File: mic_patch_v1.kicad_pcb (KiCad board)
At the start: 2 copper layers, 30 x 30 mm, 53 parts, among them J1 Conn_ARM_SWD_TagConnect_TC203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, J3 J_000001, J4 Micro_SD_Card, J5 J_000002, SW1 SW_000001, SW2 SW_000001, U1 NORA-B106-00B, U2 PWR_nPM1100-QDXX, U3 ADAU7002ACBZ-R7, Y1 CLK_0003

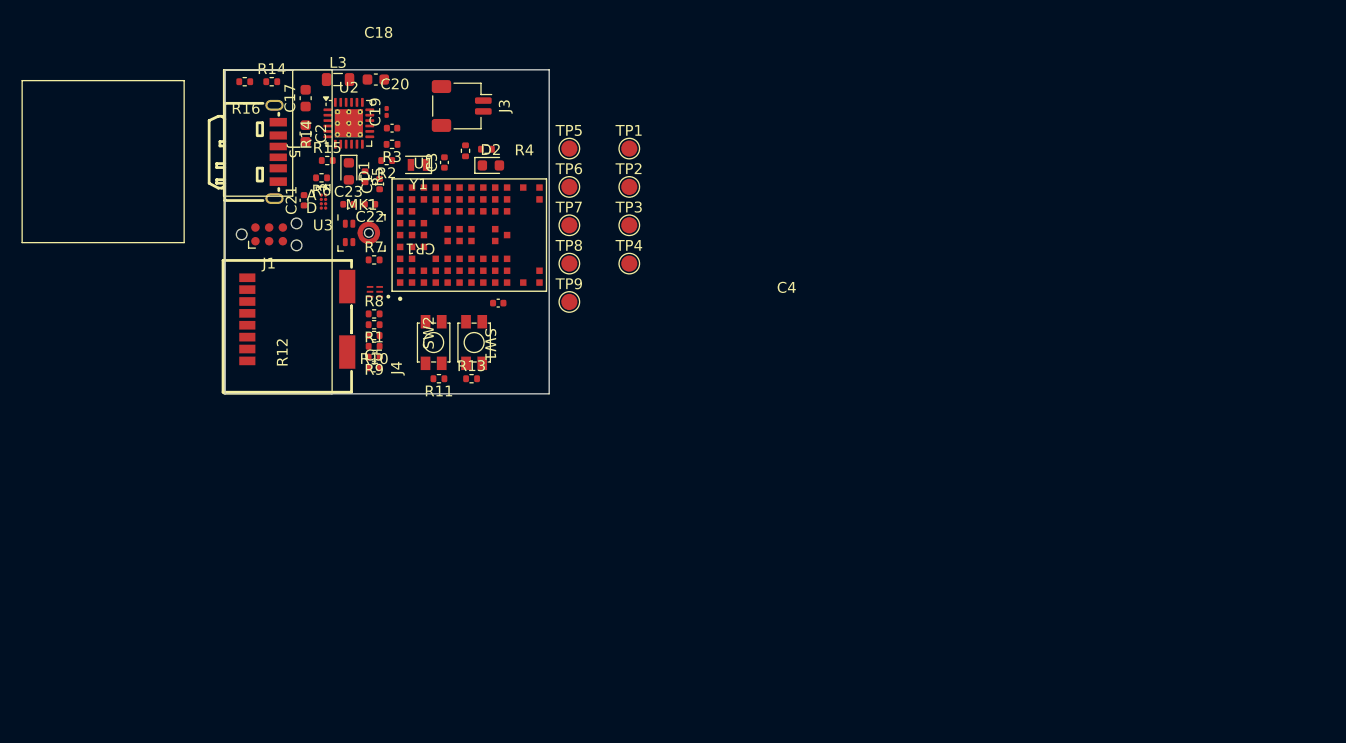
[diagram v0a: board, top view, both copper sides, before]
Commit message: sketched out board dimensions
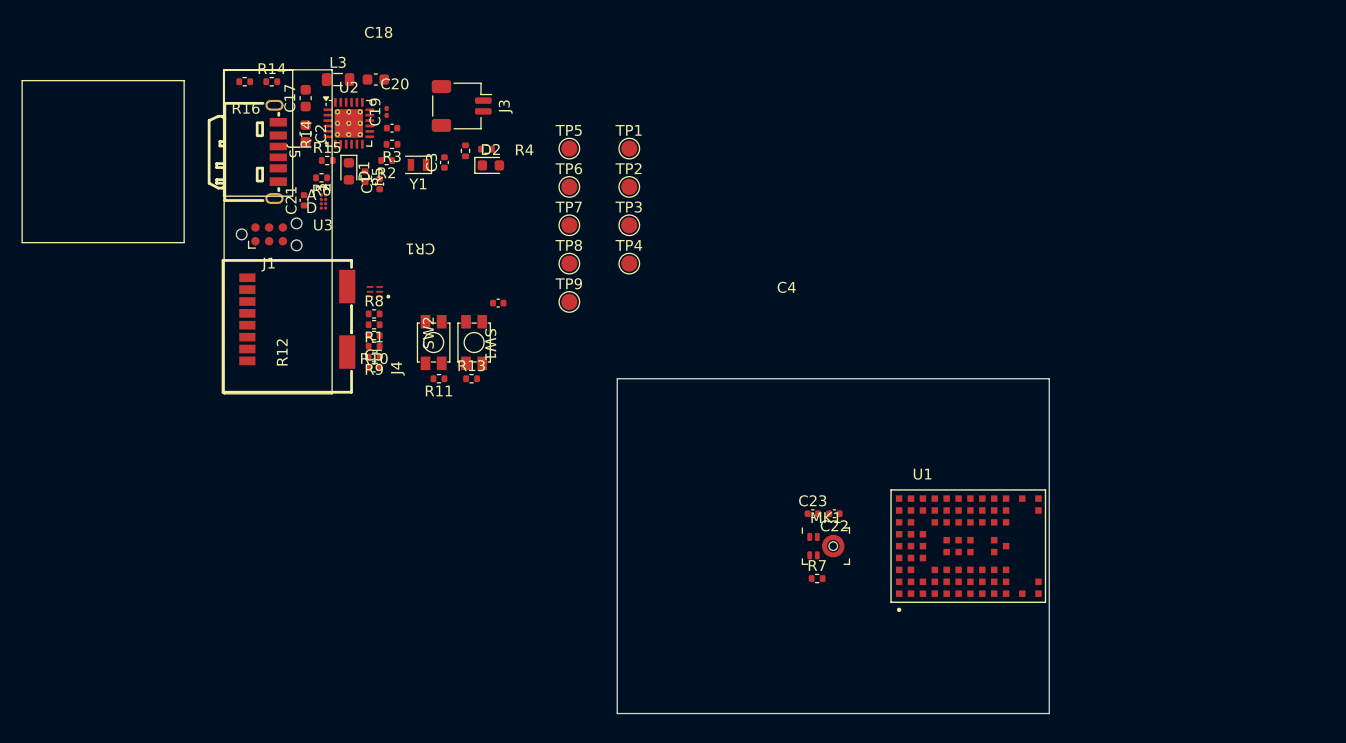
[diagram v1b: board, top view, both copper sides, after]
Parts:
- moved U1 54.4 mm to (161.6, 105.0)
- moved MK1 51.9 mm to (149.3, 105.0)
- moved C22 51.7 mm to (150.1, 102.0)
- moved C23 51.7 mm to (148.1, 102.0)
- moved R7 50.5 mm to (148.5, 108.0)
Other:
- board size 30 x 30 mm -> 40 x 31 mm

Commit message: poured ground layer added RF keep out
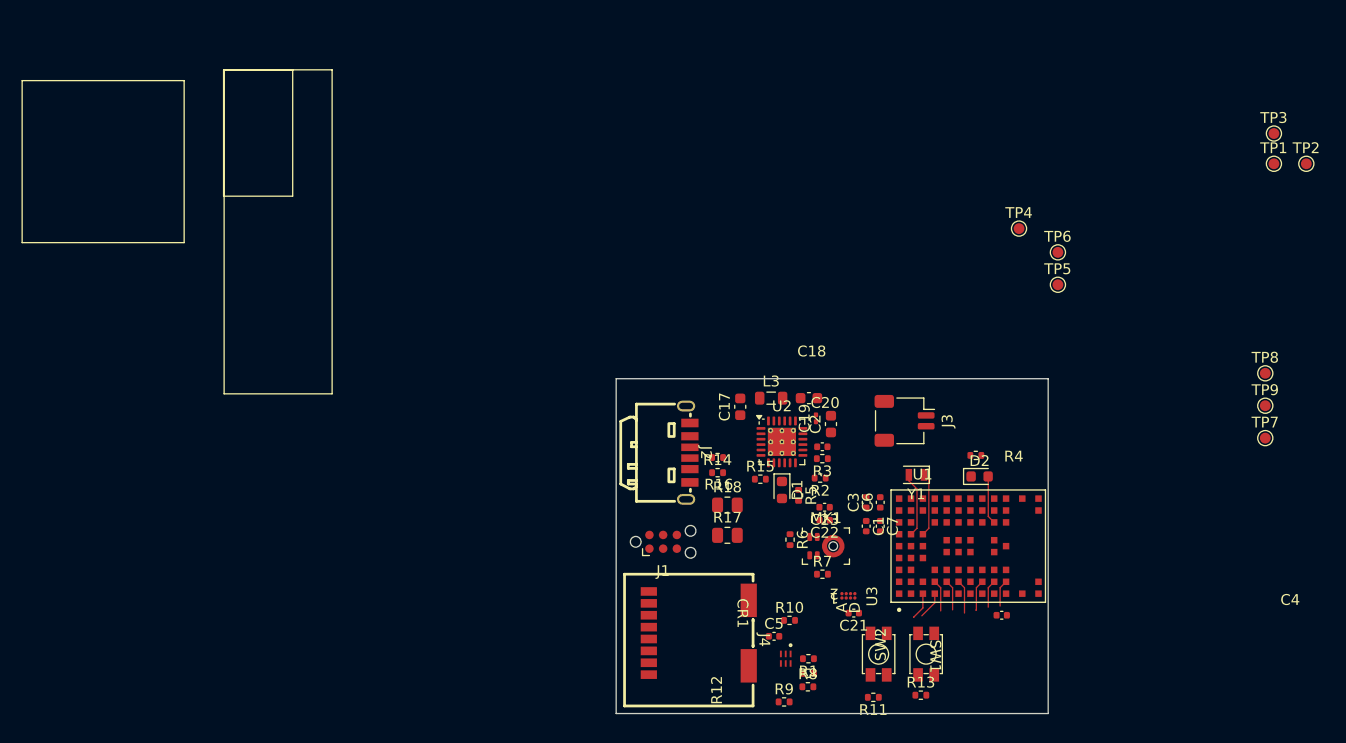
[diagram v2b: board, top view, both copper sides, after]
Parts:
- removed J5: J_000002, mic_patch_parts:C5260493
- removed the R14 at (116.0, 68.4)
- added C6: C_00001, Capacitor_SMD:C_0402_1005Metric, F.Cu at (154.3, 101.0)
- added C7: C_00001, Capacitor_SMD:C_0402_1005Metric, F.Cu at (154.3, 103.2)
- added J2: J_000002, mic_patch_parts:J_000002, F.Cu at (136.6, 96.3)
- added R17: R_00001, Resistor_SMD:R_0805_2012Metric, F.Cu at (140.2, 104.0)
- added R18: R_00001, Resistor_SMD:R_0805_2012Metric, F.Cu at (140.2, 101.2)
- TP1, TP2, TP3, TP4, TP5, TP6, TP7, TP8, TP9: footprint TestPoint:TestPoint_Pad_D1.5mm -> TestPoint:TestPoint_Pad_D1.0mm
- moved TP7 67.4 mm to (190.0, 95.0)
- moved TP8 65.2 mm to (190.0, 89.0)
- moved TP9 65.1 mm to (190.0, 92.0)
- moved C21 63.7 mm to (151.9, 111.2), turned to 180 degrees
- moved TP2 62.7 mm to (193.8, 69.6)
- moved U3 60.8 mm to (151.4, 109.6), turned to 90 degrees
- moved TP3 60.3 mm to (190.8, 66.8)
- moved TP1 59.7 mm to (190.8, 69.6)
- moved R16 55.9 mm to (139.3, 96.8)
- moved C2 55.6 mm to (149.8, 93.7), turned to 90 degrees
- moved C1 55.1 mm to (153.1, 103.2), turned to -90 degrees
- moved R14 54.9 mm to (139.3, 98.2)
- moved C4 54.9 mm to (165.6, 111.4)
- moved R6 54.8 mm to (146.0, 104.4), turned to -90 degrees
- moved Y1 54.3 mm to (157.7, 98.4)
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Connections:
- C18 pad 1: /Power/DEC_NPM -> GND
- C18 pad 2: GND -> /Power/DEC_NPM
- J4 pad 9: unconnected-(J4-SHIELD-Pad9) -> GND
- U2 pad 2: VSYS -> Net-(U2-VOUTBSET0)
- U2 pad 3: VSYS -> Net-(U2-VOUTBSET0)
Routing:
- net Net-(U1-P0.01/XL2): track 0.00 -> 6.04 mm
- net Net-(U1-P0.00/XL1): track 0.00 -> 5.91 mm
- net Net-(D2-A): track 0.00 -> 4.64 mm
- net FSYNC_LRCLK: track 0.00 -> 3.13 mm
- net DIN: track 0.00 -> 2.93 mm
- net /MCU/SWDIO: track 0.00 -> 2.90 mm
- net BCLK: track 0.00 -> 2.83 mm
- net /MCU/SWCLK: track 0.00 -> 2.58 mm
- net SD MISO: track 0.00 -> 2.55 mm
- net SD CSN: track 0.00 -> 2.55 mm
- net GND: track 0.00 -> 2.48 mm
- added copper zone on In1.Cu, net GND
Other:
- copper layers 2 -> 4

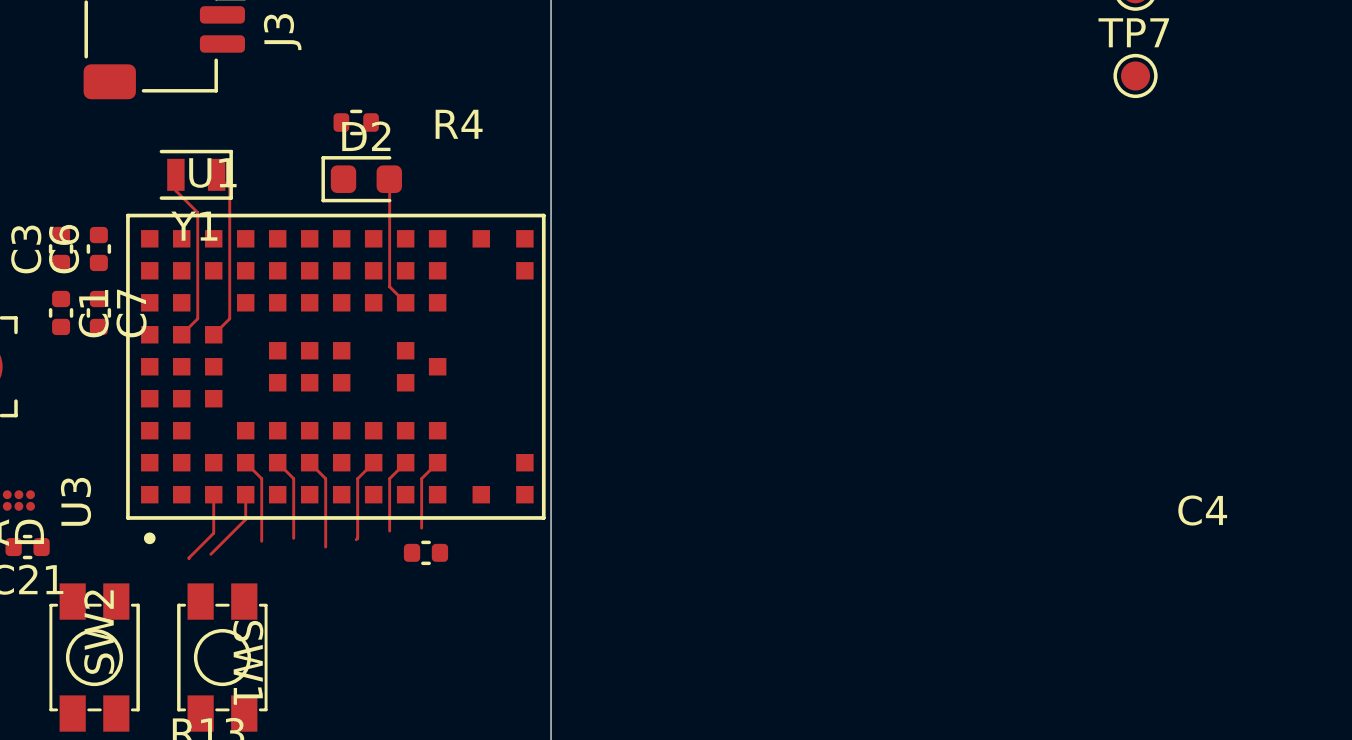
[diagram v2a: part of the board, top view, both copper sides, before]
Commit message: added RF ground plane stitching vias
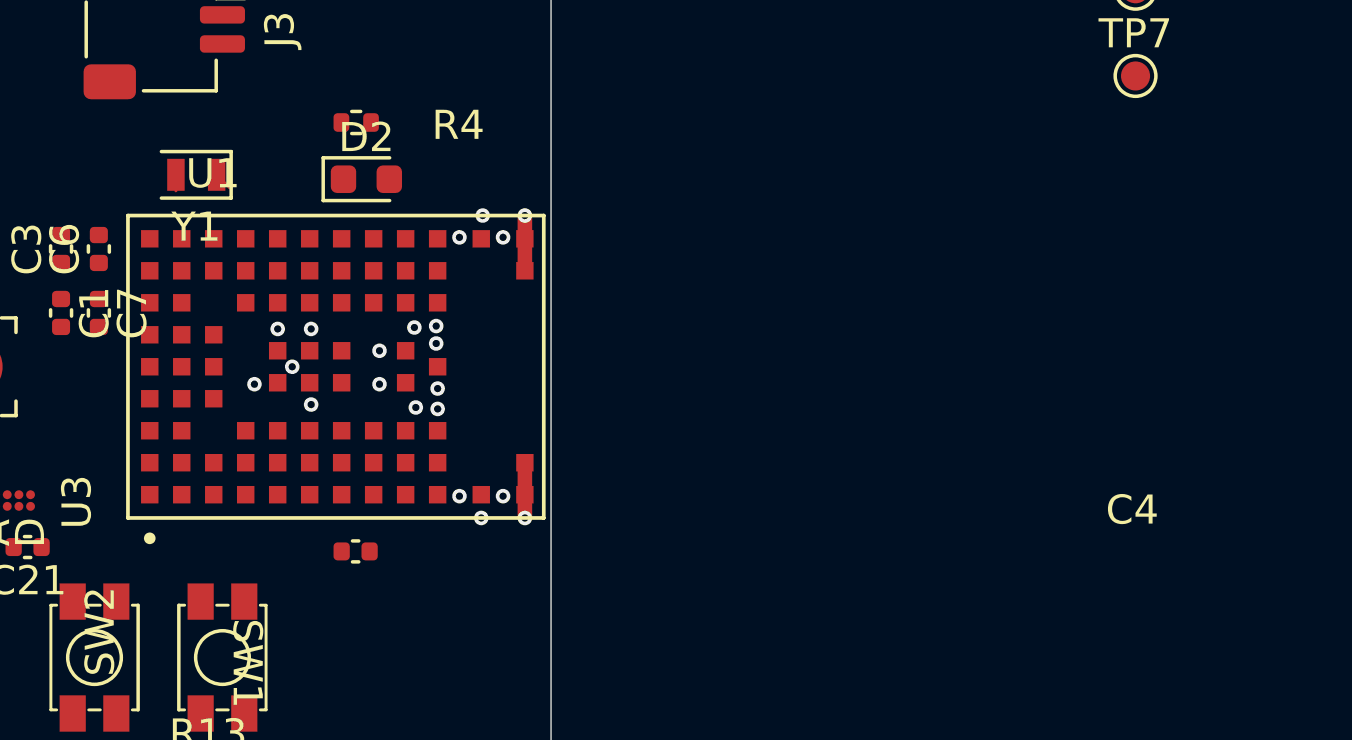
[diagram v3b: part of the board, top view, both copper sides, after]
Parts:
- moved C4 2.42 mm to (163.2, 111.3)
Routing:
- net Net-(U1-P0.01/XL2): track 6.04 -> 0.55 mm
- net Net-(U1-P0.00/XL1): track 5.91 -> 0.64 mm
- net Net-(D2-A): track 4.64 -> 0.05 mm
- net FSYNC_LRCLK: track 3.13 -> 0.00 mm
- net DIN: track 2.93 -> 0.00 mm
- net /MCU/SWDIO: track 2.90 -> 0.00 mm
- net BCLK: track 2.83 -> 0.00 mm
- net /MCU/SWCLK: track 2.58 -> 0.00 mm
- net SD MISO: track 2.55 -> 0.00 mm
- net SD CSN: track 2.55 -> 0.00 mm
- net GND: track 2.48 -> 3.80 mm, vias 0 -> 21

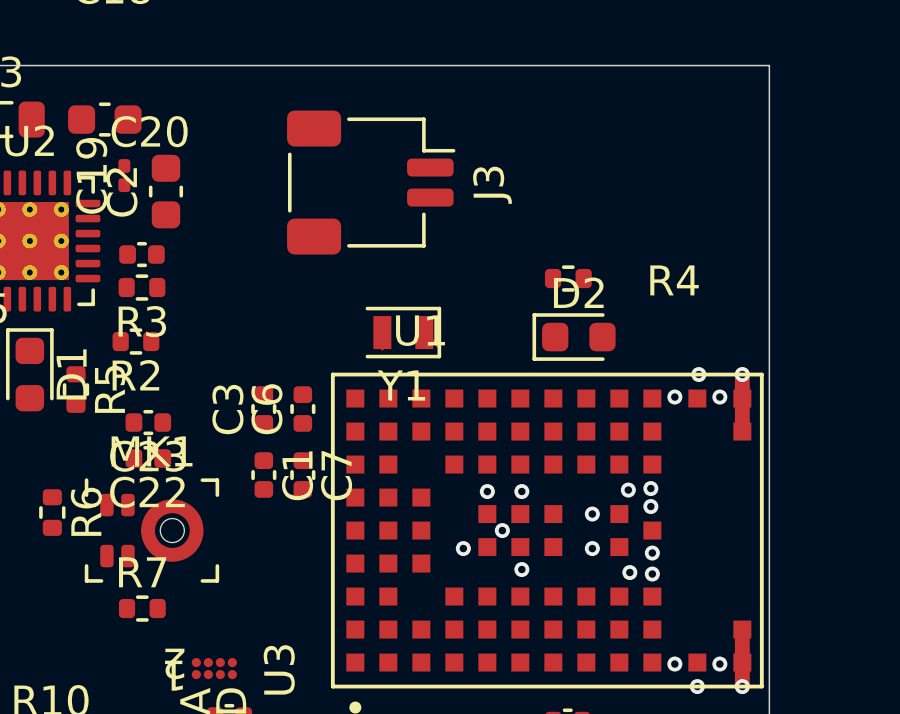
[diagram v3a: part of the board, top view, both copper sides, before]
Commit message: switched around pins for easier routing
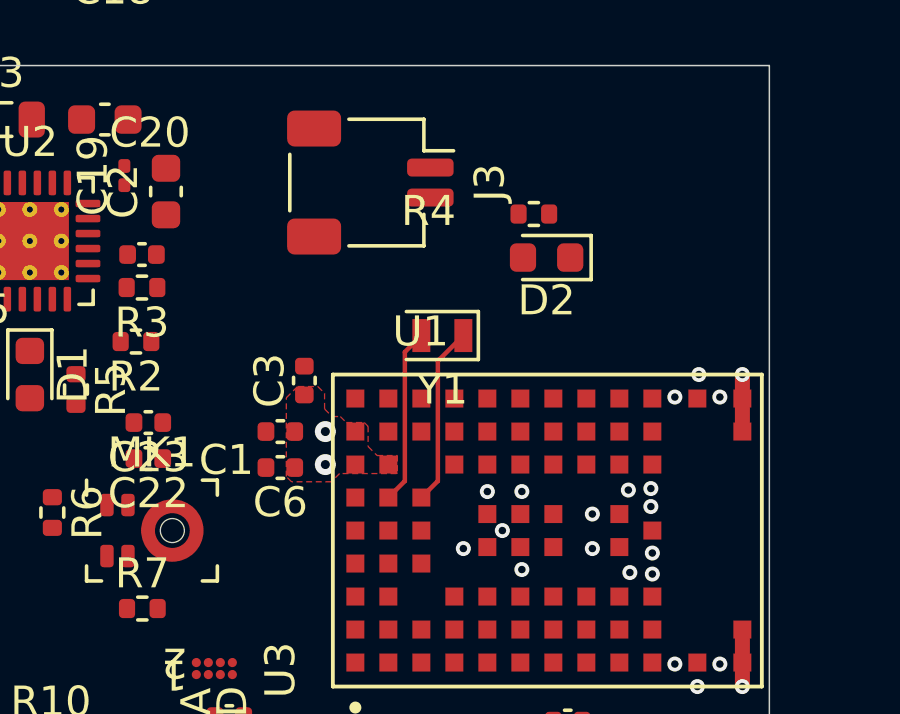
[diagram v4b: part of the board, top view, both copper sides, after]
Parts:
- removed C7: C_00001, Capacitor_SMD:C_0402_1005Metric
- moved D2 2.86 mm to (162.5, 95.9), turned to 180 degrees
- moved R4 2.44 mm to (162.1, 94.5), turned to 180 degrees
- moved C6 2.09 mm to (153.6, 102.9), turned to 180 degrees
- moved C3 1.65 mm to (154.4, 100.0)
- moved C1 1.55 mm to (153.6, 101.7), turned to 180 degrees
- moved Y1 1.30 mm to (159.0, 98.5)
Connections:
- U1 pad F9: unconnected-(U1-P1.15-PadF9) -> NPM ERROR
- U1 pad G4: NPM ERROR -> unconnected-(U1-P1.04-PadG4)
- U1 pad G9: unconnected-(U1-P1.13-PadG9) -> Net-(D2-A)
- U1 pad J7: Net-(D2-A) -> unconnected-(U1-P1.10-PadJ7)
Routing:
- net Net-(U1-P0.00/XL1): track 0.64 -> 5.98 mm
- net Net-(U1-P0.01/XL2): track 0.55 -> 5.86 mm
- net +3V0 VDD_NRF: vias 0 -> 2
- added copper zone on F.Cu, net +3V0 VDD_NRF

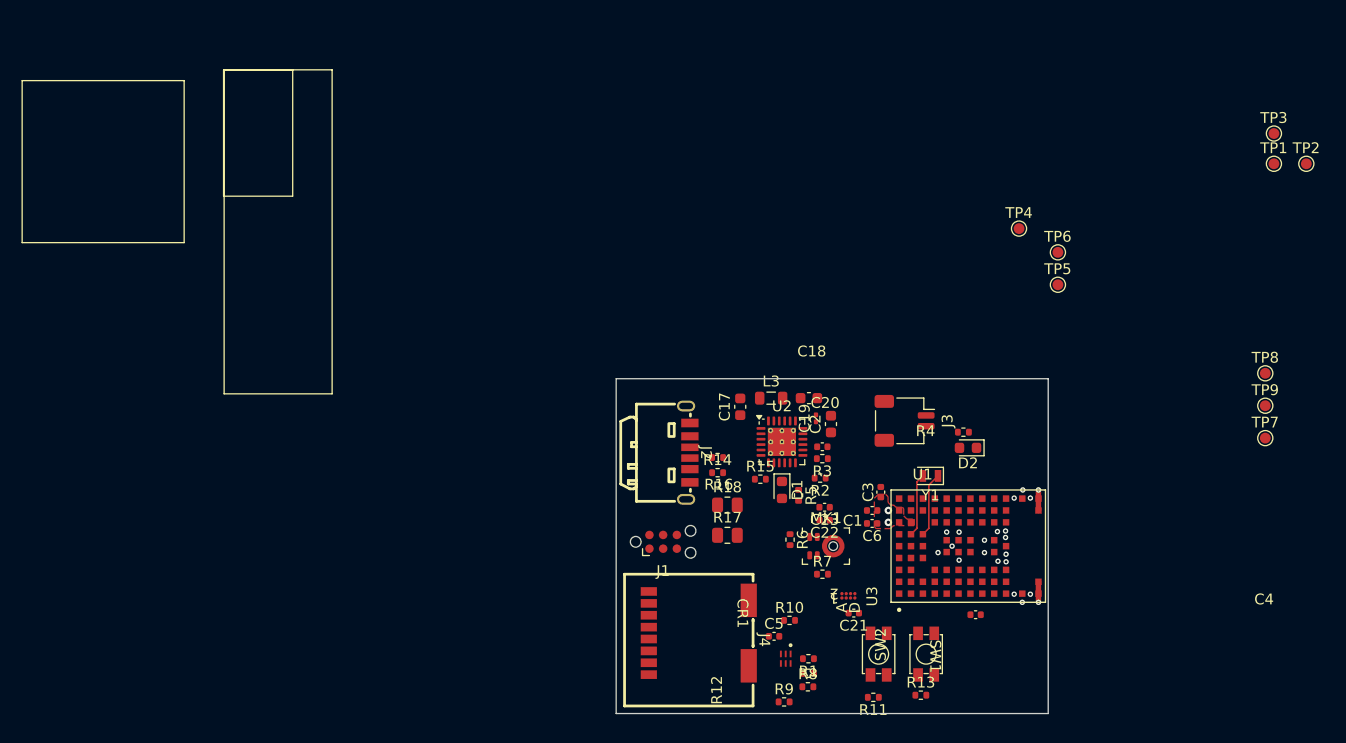
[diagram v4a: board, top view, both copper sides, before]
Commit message: routed audio
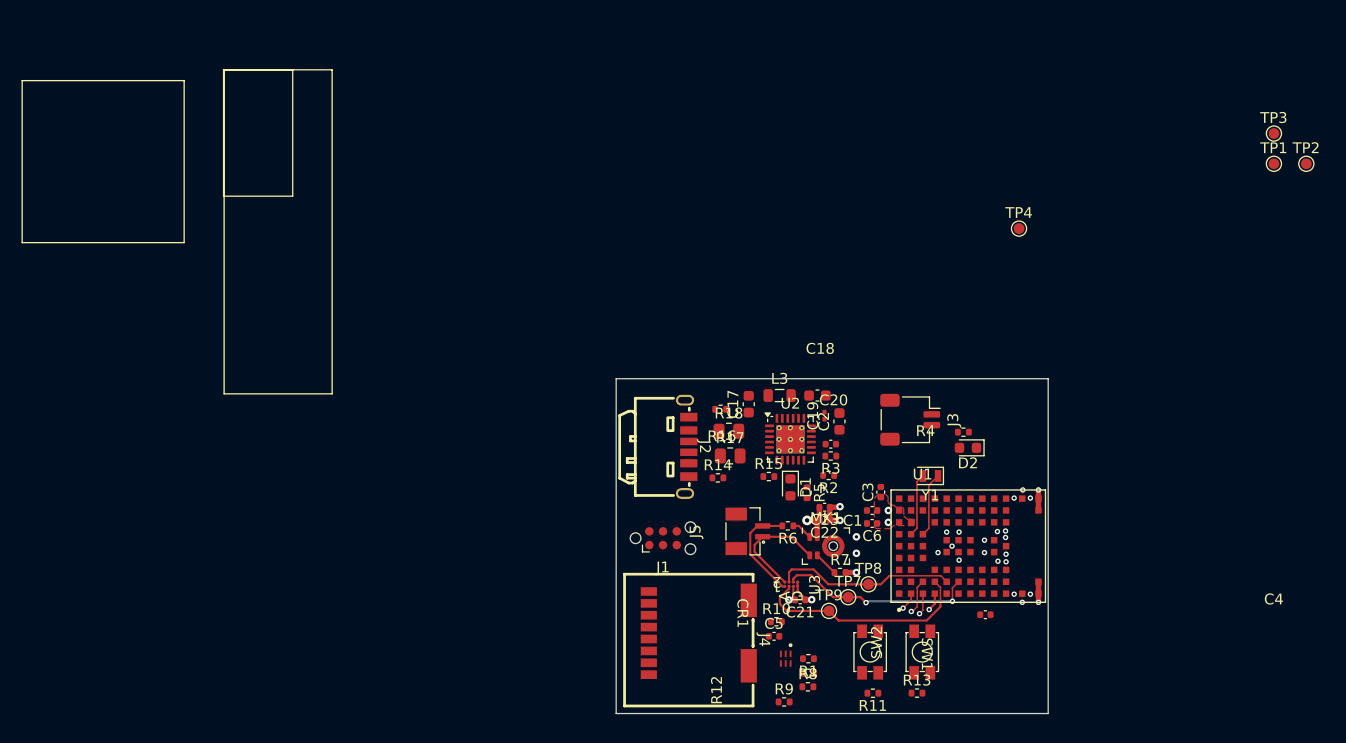
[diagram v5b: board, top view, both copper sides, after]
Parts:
- removed TP5: TestPoint PDM DAT, TestPoint:TestPoint_Pad_D1.0mm
- removed TP6: TestPoint PDM CLK, TestPoint:TestPoint_Pad_D1.0mm
- added J5: J_000003, mic_patch_parts:J_00003, F.Cu at (142.2, 103.6)
- moved TP9 44.6 mm to (149.6, 111.0)
- moved TP8 41.6 mm to (153.3, 108.5)
- moved TP7 41.3 mm to (151.4, 109.7)
- moved R17 7.36 mm to (140.5, 96.6)
- moved R18 6.84 mm to (140.3, 94.4)
- moved U3 5.40 mm to (146.1, 108.5)
- moved C21 5.11 mm to (146.9, 110.0)
- moved R16 4.48 mm to (139.6, 92.3)
- moved R7 1.63 mm to (150.6, 107.4)
- moved R6 1.29 mm to (145.8, 103.1), turned to 180 degrees
- moved R10 1.22 mm to (144.7, 112.0)
- moved C4 0.90 mm to (164.1, 111.3)
- moved C17 0.82 mm to (142.2, 91.9)
- moved C19 0.82 mm to (149.2, 92.9)
- moved C2 0.82 mm to (150.6, 93.5)
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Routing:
- net DIN: track 0.00 -> 20.5 mm
- net FSYNC_LRCLK: track 0.00 -> 18.3 mm, vias 0 -> 2
- net BCLK: track 0.00 -> 16.7 mm
- net /Mic/PDM_CLK: track 0.00 -> 10.7 mm
- net /Mic/PDM_DAT: track 0.00 -> 9.63 mm
- net +3V0 VDD_NRF: track 0.00 -> 6.57 mm, vias 2 -> 4
- net GND: track 3.80 -> 9.86 mm, vias 21 -> 27
- net SD MOSI: track 0.00 -> 3.26 mm, vias 0 -> 1
- net /Mic/L_R: track 0.00 -> 2.25 mm
- net SD MISO: track 0.00 -> 1.98 mm, vias 0 -> 1
- net Net-(MK1-DATA): track 0.00 -> 1.94 mm
- net SD CSN: track 0.00 -> 1.70 mm, vias 0 -> 1
- net SD SCLK: track 0.00 -> 1.65 mm, vias 0 -> 1
